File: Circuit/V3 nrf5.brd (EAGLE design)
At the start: 45.1 x 52.7 mm, 54 parts, among them J4 USB Micro, J7 CORTEX_DEBUG_SMD, Q2 BSS84, U1 74AHCT2G125, U2 MCP73831, U3 BC840M, U4 MIC5205, U8 TPS61235P, Y1 32.768kHz

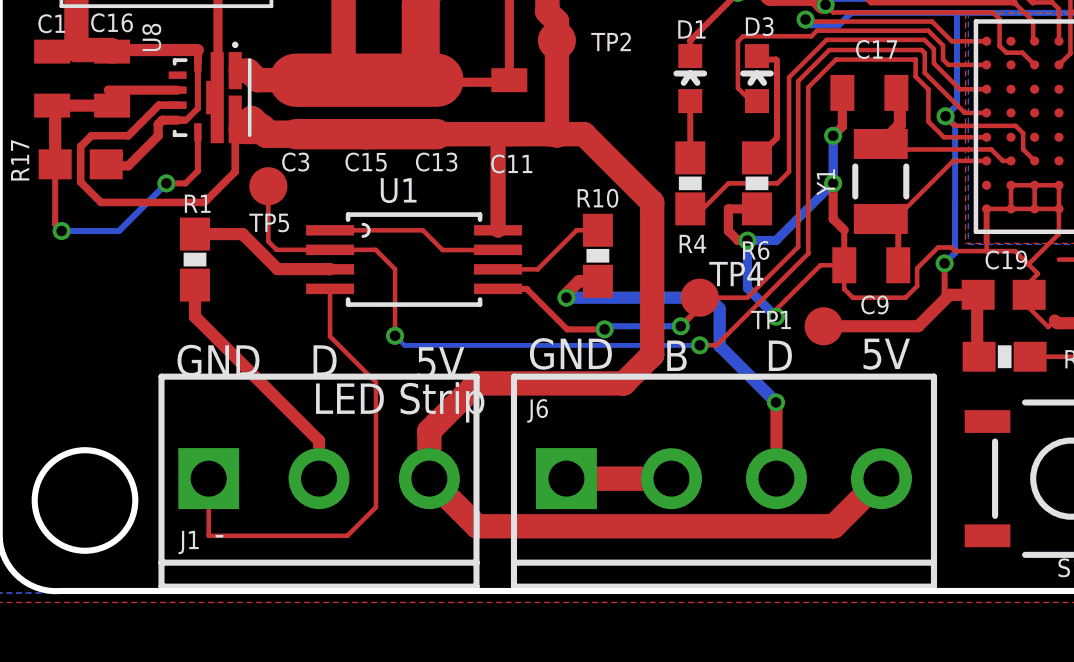
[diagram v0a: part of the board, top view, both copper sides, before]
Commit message: Moving from millis timealive to seconds timealive.
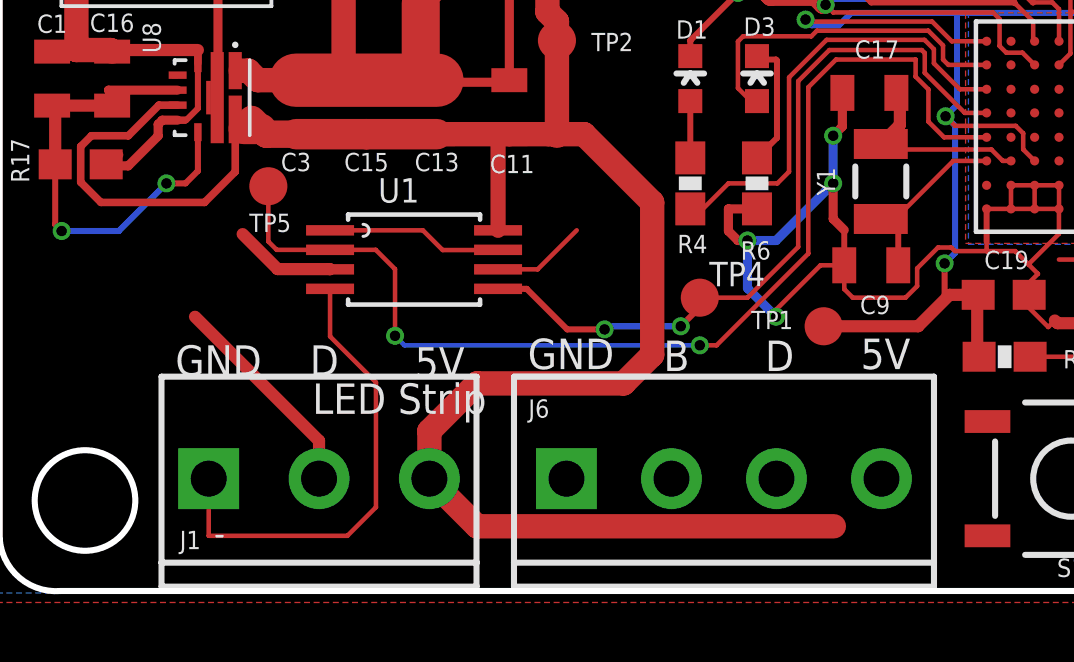
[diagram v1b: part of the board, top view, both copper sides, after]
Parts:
- removed R1, R10: 330, SparkFun:0603-RES
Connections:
- removed net N$17: J1.2, R1.1
- removed net N$2: J6.3, R10.1
- net 5V: now also J6.1; no longer J6.4
- net HEADLAMP_5V: now also J1.2; no longer R1.2
- net N$9: now also J6.3, J6.4; no longer J6.1, J6.2
- net STRIP_5V: now also J6.2; no longer R10.2
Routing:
- net N$2: track 13.1 -> 0.00 mm, vias 2 -> 0
- net N$17: track 8.17 -> 0.00 mm
- net HEADLAMP_5V: track 4.99 -> 10.5 mm
- net N$9: track 3.50 -> 0.00 mm
- net 5V: track 85.9 -> 83.7 mm
- net STRIP_5V: track 3.87 -> 3.16 mm
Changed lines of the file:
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@@
 <attribute name="VALUE" x="13.6525" y="1.4605" size="0.6096" layer="27" font="vector" ratio="20"/>
-</element>
-<element name="R10" library="SparkFun" package="0603-RES" value="330" x="15.97025" y="11.557" smashed="yes" rot="R90">
-<attribute name="DIGIKEY" value="P330HCT-ND" x="15.97025" y="11.557" size="1.778" layer="27" rot="R90" display="off"/>
-<attribute name="NAME" x="16.7005" y="13.7795" size="0.6096" layer="25" font="vector" rot="R180"/>
-<attribute name="VALUE" x="17.11325" y="10.541" size="0.4064" layer="27" font="vector" rot="R90"/>
 </element>
 <element name="J7" library="SparkFun-Connectors" library_urn="urn:adsk.eagle:library:513" package="SAMTECH_FTSH-105-01" package3d_urn="urn:adsk.eagle:package:38289/1" value="CORTEX_DEBUG_SMD" x="32.258" y="29.083" smashed="yes" rot="R90">
@@
 <attribute name="SF_ID" value="PRT-08235" x="3.175" y="4.1275" size="1.778" layer="27" display="off"/>
 <attribute name="VALUE" x="5.08" y="-0.5715" size="0.6096" layer="27" font="vector" ratio="20"/>
-</element>
-<element name="R1" library="SparkFun" package="0603-RES" value="330" x="2.54" y="11.43" smashed="yes" rot="R90">
-<attribute name="DIGIKEY" value="P330HCT-ND" x="2.54" y="11.43" size="1.778" layer="27" rot="R90" display="off"/>
-<attribute name="NAME" x="2.12725" y="12.98575" size="0.6096" layer="25" font="vector"/>
-<attribute name="VALUE" x="3.683" y="10.414" size="0.4064" layer="27" font="vector" rot="R90"/>
 </element>
 <element name="U1" library="cdclvc11xx_10" package="TSSOP8" value="74AHCT2G125" x="9.8425" y="11.43" smashed="yes" rot="R270">
@@
 </signal>
 <signal name="STRIP_5V">
-<contactref element="R10" pad="2"/>
 <contactref element="U1" pad="6"/>
 <wire x1="12.6425" y1="11.105" x2="13.9625" y2="11.105" width="0.1524" layer="1"/>
-<wire x1="15.2645" y1="12.407" x2="15.97025" y2="12.407" width="0.1524" layer="1"/>
 <wire x1="13.9625" y1="11.105" x2="15.2645" y2="12.407" width="0.1524" layer="1"/>
+<contactref element="J6" pad="2"/>
+<wire x1="18.4225" y1="4.1275" x2="15.2645" y2="12.407" width="0" layer="19" extent="1-1"/>
 </signal>
 <signal name="5V">
@@
 <wire x1="4.1275" y1="16.1025" x2="3.8815" y2="16.1025" width="0.2032" layer="1"/>
 <wire x1="4.7461" y1="15.785" x2="4.1619" y2="15.785" width="1.016" layer="1"/>
-<contactref element="J6" pad="4"/>
-<wire x1="25.4225" y1="4.1275" x2="23.835" y2="2.54" width="0.8128" layer="1"/>
 <wire x1="11.9403" y1="2.54" x2="10.3528" y2="4.1275" width="0.8128" layer="1"/>
 <wire x1="23.835" y1="2.54" x2="11.9403" y2="2.54" width="0.8128" layer="1"/>
@@
 <wire x1="12.6425" y1="12.405" x2="12.6425" y2="15.5525" width="0.508" layer="1"/>
 <wire x1="12.6425" y1="15.5525" x2="12.7" y2="15.61" width="0.508" layer="1"/>
+<contactref element="J6" pad="1"/>
+<wire x1="10.3528" y1="4.1275" x2="14.9225" y2="4.1275" width="0" layer="19" extent="1-1"/>
 </signal>
 <signal name="STRIP_3V3">
@@
 </signal>
 <signal name="HEADLAMP_5V">
-<contactref element="R1" pad="2"/>
 <contactref element="U1" pad="3"/>
 <wire x1="7.0425" y1="11.105" x2="7.035" y2="11.1125" width="0.4064" layer="1"/>
 <wire x1="5.295" y1="11.1125" x2="4.1275" y2="12.28" width="0.4064" layer="1"/>
-<wire x1="4.1275" y1="12.28" x2="2.54" y2="12.28" width="0.4064" layer="1"/>
 <wire x1="7.035" y1="11.1125" x2="5.295" y2="11.1125" width="0.4064" layer="1"/>
-</signal>
-<signal name="N$17">
-<contactref element="R1" pad="1"/>
 <contactref element="J1" pad="2"/>
 <wire x1="6.675" y1="4.1275" x2="6.675" y2="5.39" width="0.4064" layer="1"/>
-<wire x1="2.54" y1="9.525" x2="2.54" y2="10.58" width="0.4064" layer="1"/>
 <wire x1="6.675" y1="5.39" x2="2.54" y2="9.525" width="0.4064" layer="1"/>
+<wire x1="2.54" y1="9.525" x2="4.1275" y2="12.28" width="0" layer="19" extent="1-1"/>
 </signal>
 <signal name="N$9">
-<contactref element="J6" pad="2"/>
-<contactref element="J6" pad="1"/>
-<wire x1="14.9225" y1="4.1275" x2="18.4225" y2="4.1275" width="0.8128" layer="1"/>
-</signal>
-<signal name="N$2">
 <contactref element="J6" pad="3"/>
-<contactref element="R10" pad="1"/>
-<wire x1="15.33525" y1="10.707" x2="15.331625" y2="10.703375" width="0.2032" layer="1"/>
-<via x="14.9225" y="10.16" extent="1-16" drill="0.35"/>
-<via x="21.9075" y="6.6675" extent="1-16" drill="0.35"/>
-<wire x1="15.97025" y1="10.707" x2="15.33525" y2="10.707" width="0.4064" layer="1"/>
-<wire x1="15.331625" y1="10.703375" x2="14.9225" y2="10.29425" width="0.4064" layer="1"/>
-<wire x1="14.9225" y1="10.29425" x2="14.9225" y2="10.16" width="0.4064" layer="1"/>
-<wire x1="19.0951125" y1="10.1826" x2="19.6398875" y2="10.1826" width="0.4064" layer="16"/>
-<wire x1="19.6398875" y1="10.1826" x2="20.0251" y2="9.7973875" width="0.4064" layer="16"/>
-<wire x1="20.0251" y1="8.5499" x2="21.9075" y2="6.6675" width="0.4064" layer="16"/>
-<wire x1="19.0725125" y1="10.16" x2="19.0951125" y2="10.1826" width="0.4064" layer="16"/>
-<wire x1="14.9225" y1="10.16" x2="19.0725125" y2="10.16" width="0.4064" layer="16"/>
-<wire x1="20.0251" y1="9.7973875" x2="20.0251" y2="8.5499" width="0.4064" layer="16"/>
-<wire x1="21.9075" y1="6.6675" x2="21.9225" y2="6.6525" width="0.4064" layer="1"/>
-<wire x1="21.9225" y1="6.6525" x2="21.9225" y2="4.1275" width="0.4064" layer="1"/>
+<contactref element="J6" pad="4"/>
+<wire x1="21.9225" y1="4.1275" x2="25.4225" y2="4.1275" width="0" layer="19" extent="1-1"/>
 </signal>
 </signals>

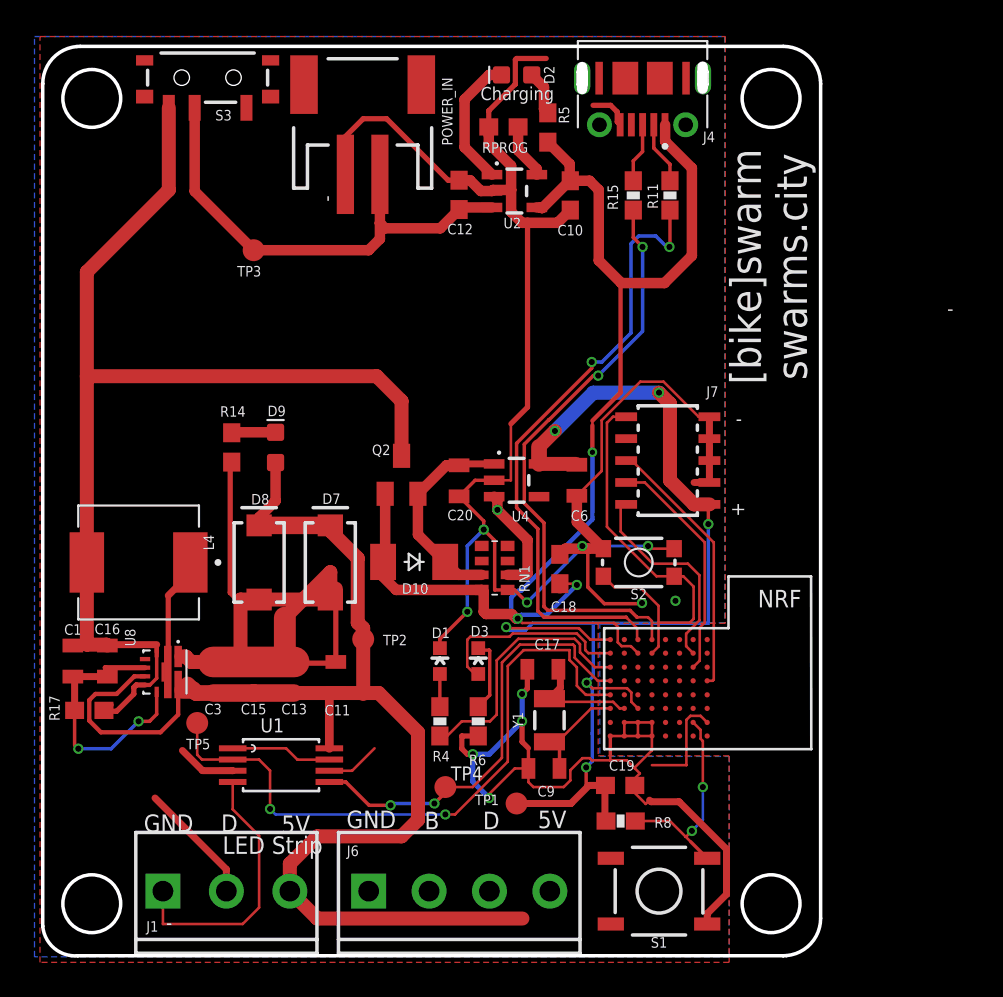
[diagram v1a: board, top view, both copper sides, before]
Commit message: updated footprints level-shifter, cystral and connetors
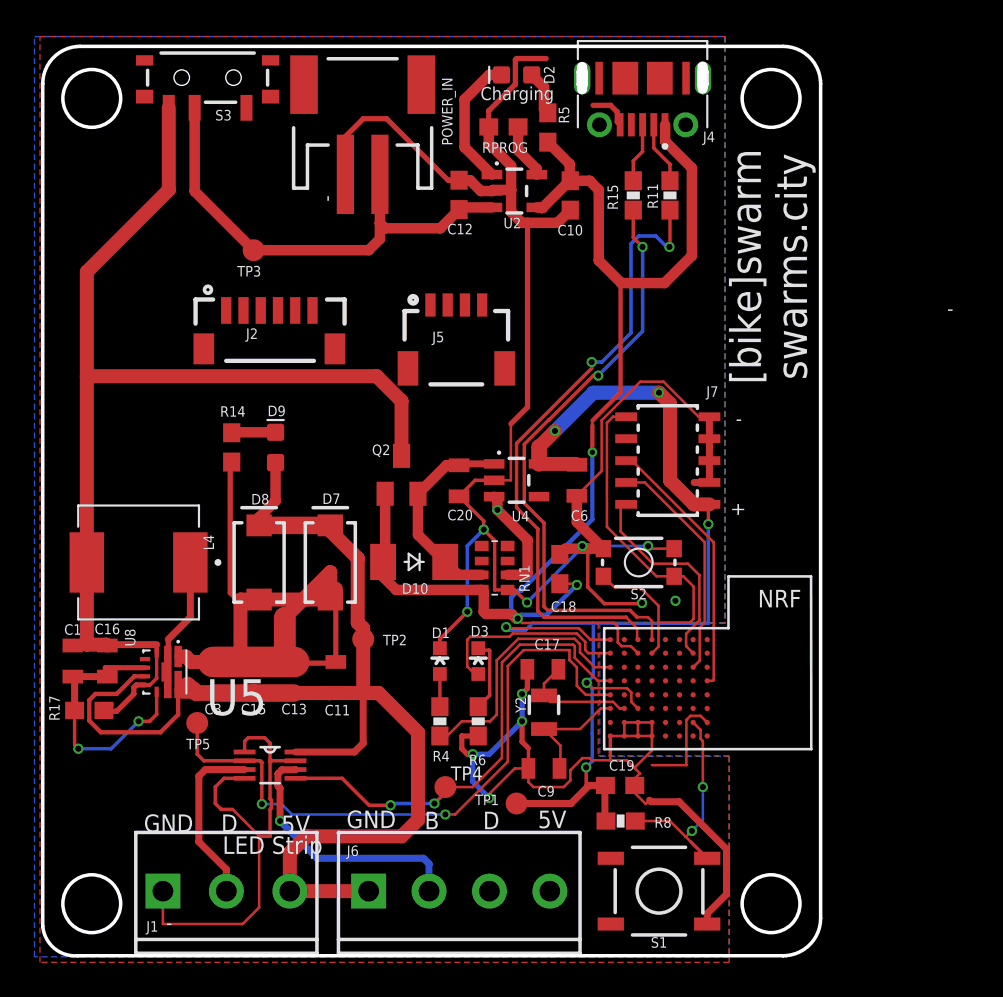
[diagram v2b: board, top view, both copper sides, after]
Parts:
- removed U1: 74AHCT2G125, cdclvc11xx_10:TSSOP8
- removed Y1: 32.768kHz, SparkFun-Clocks:CRYSTAL-SMD-3.2X1.5MM
- added J2: (no value), SparkFun-Connectors:1X06-1MM
- added J5: (no value), SparkFun-Connectors:1X04_1MM_RA
- added U5: 74AHCT2G125, VSSOP8:VSSOP-8
- added Y2: (no value), SparkFun-Clocks:CYSTAL-SMD-2X1.2MM
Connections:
- removed net N$10: C9.1, U3.F7, Y1.P$2
- removed net N$8: C17.1, U3.F6, Y1.P$1
- new net N$17: C17.1, U3.F6, Y2.P$2
- new net N$2: C9.1, U3.F7, Y2.P$1
- new net PIN_01: J2.3, U3.D1
- new net PIN_02: J2.4, U3.E0
- new net PIN_03: J2.5, U3.E1
- new net PIN_04: J2.6, U3.F4
- new net SCL: J5.4, U3.D6
- new net SDA: J5.3, U3.E6
- net 3.3V: now also J2.2, J5.2
- net 5V: now also U5.8_VCC; no longer U1.8
- net GND: now also J2.1, J5.1, U5.1_1!OE, U5.4_GND, U5.7_2!OE; no longer U1.1, U1.4, U1.7
- net HEADLAMP_3V3: now also U5.5_2A; no longer U1.5
- net HEADLAMP_5V: now also U5.3_2Y; no longer U1.3
- net STRIP_3V3: now also U5.2_1A; no longer U1.2
- net STRIP_5V: now also U5.6_1Y; no longer U1.6
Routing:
- net STRIP_5V: track 3.16 -> 15.1 mm, vias 0 -> 1
- net 5V: track 83.7 -> 75.5 mm
- net N$10: track 7.87 -> 0.00 mm
- net N$2: track 0.00 -> 7.04 mm
- net N$17: track 0.00 -> 6.83 mm
- net N$8: track 6.59 -> 0.00 mm
- net GND: track 258.7 -> 265.2 mm
- net HEADLAMP_3V3: track 25.6 -> 27.7 mm

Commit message: V8 of the board, ready to print.
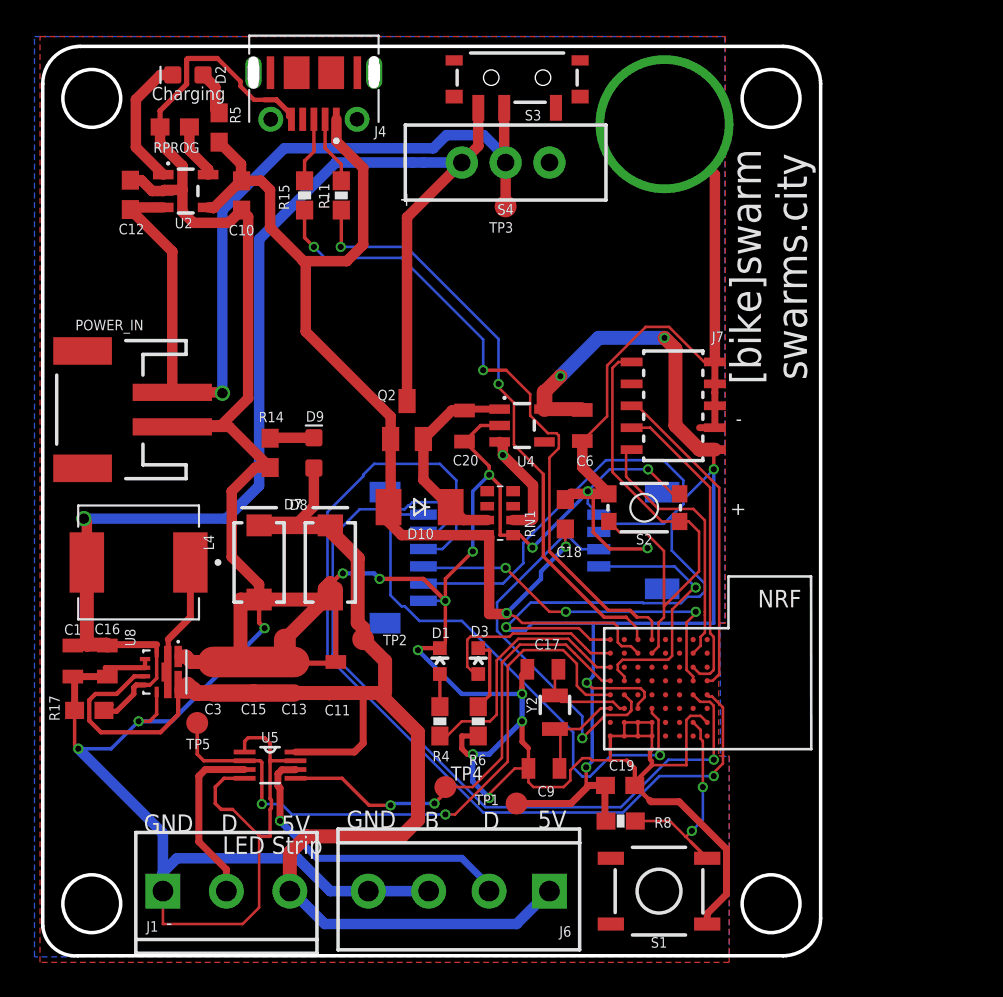
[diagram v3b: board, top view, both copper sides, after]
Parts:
- added S4: (no value), SparkFun-Switches:SWITCH_SPDT_PTH_11.6X4.0MM
- moved POWER_IN 22.7 mm to (-0.16, 32.0), turned to 90 degrees
- moved J4 19.1 mm to (11.7, 51.2)
- moved C10 19.1 mm to (7.56, 44.5)
- moved D2 19.1 mm to (4.45, 51.4)
- moved R15 19.1 mm to (11.2, 44.5)
- moved RPROG 19.1 mm to (3.68, 48.4)
- moved C12 19.0 mm to (1.11, 44.5)
- moved R11 19.0 mm to (13.3, 44.5)
- moved R5 19.0 mm to (6.25, 48.4)
- moved U2 19.0 mm to (4.32, 44.7)
- moved S3 17.9 mm to (23.5, 51.3)
- moved J5 16.0 mm to (28.3, 24.4), flipped to the bottom, turned to 270 degrees
- moved J2 15.1 mm to (16.8, 23.5), flipped to the bottom, turned to 90 degrees
- moved TP3 14.8 mm to (22.9, 43.8)
- moved J6 10.5 mm to (25.4, 4.13), turned to 180 degrees
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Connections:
- removed net N$9: J6.3, J6.4
- removed net VBAT_S: C12.1, POWER_IN.2, S3.2, TP3.TP, U2.3
- new net VBAT_RAW: C12.1, POWER_IN.2, S3.2, S4.2, TP3.TP, U2.3
- net GND: now also J6.3, J6.4
- net VBAT: now also S4.1
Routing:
- net GND: track 265.2 -> 338.8 mm, vias 13 -> 18
- net PIN_02: track 0.00 -> 55.3 mm, vias 0 -> 1
- net VBAT_RAW: track 0.00 -> 52.1 mm, vias 0 -> 1
- net 3.3V: track 67.4 -> 117.9 mm
- net PIN_03: track 0.00 -> 48.6 mm, vias 0 -> 1
- net PIN_04: track 0.00 -> 30.8 mm, vias 0 -> 1
- net VBAT_S: track 28.2 -> 0.00 mm
- net SDA: track 0.00 -> 22.2 mm, vias 0 -> 1
- net PIN_01: track 0.00 -> 21.4 mm, vias 0 -> 3
- net 5V: track 75.5 -> 91.1 mm
- net SCL: track 0.00 -> 15.6 mm, vias 0 -> 1
- net VBAT: track 68.0 -> 77.8 mm, vias 0 -> 1
- net VBUS: track 80.1 -> 70.3 mm, vias 3 -> 2
- net SWDCLK: track 13.5 -> 18.1 mm
- net RESET: track 24.9 -> 29.3 mm
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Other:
- board text added: "[bike]swarm V8 5/24/2021 swarms.city"
- board text removed: "[bike]swarm V7 4/11/2021 swarms.city"

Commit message: Updating 10 components to different digikey values. A few changes, such as MIC5209 -> MIC5317.
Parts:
- U4: value MIC5205 -> MIC5317 (MIC5205)
- Y2: value (none) -> FC-12M; device SparkFun-Clocks:CYSTAL-SMD-2X1.2MM -> crystal:FC-12M
- moved Y2 0.63 mm to (25.7, 14.3)
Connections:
- net N$17: now also Y2.2; no longer Y2.P$2
- net N$2: now also Y2.1; no longer Y2.P$1
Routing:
- net N$2: track 6.14 -> 6.67 mm

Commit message: update board
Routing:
- net D+: track 38.5 -> 37.6 mm
- net 5V: track 91.1 -> 90.5 mm
- net HEADLAMP_5V: track 10.1 -> 9.64 mm
